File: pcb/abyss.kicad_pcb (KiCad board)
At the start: 2 copper layers, 137.5 x 111.5 mm, 36 parts

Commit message: Fix nets
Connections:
- D14 pad 1: R4 -> R3
- D15 pad 1: R4 -> R3
- D16 pad 1: R4 -> R3

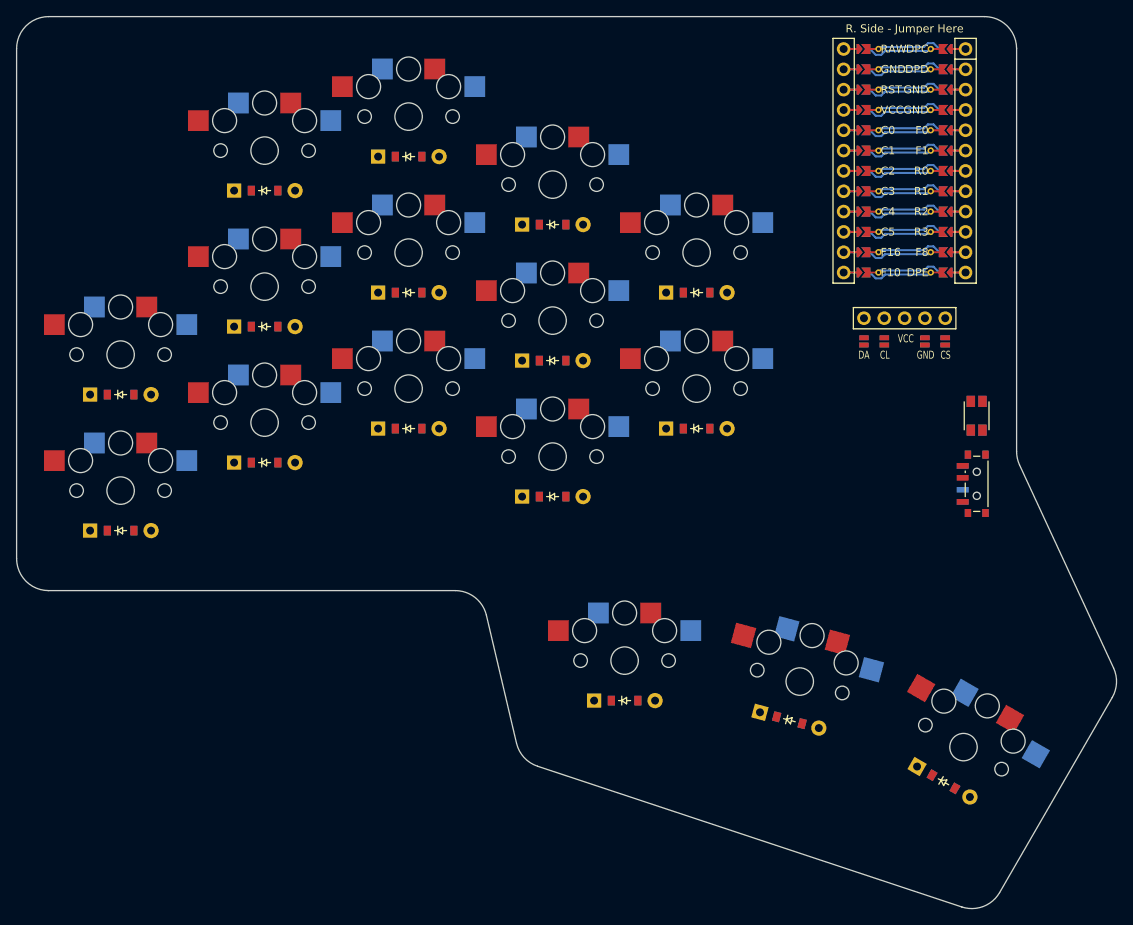
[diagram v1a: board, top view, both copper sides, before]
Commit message: Add battery jst and cleanup layout
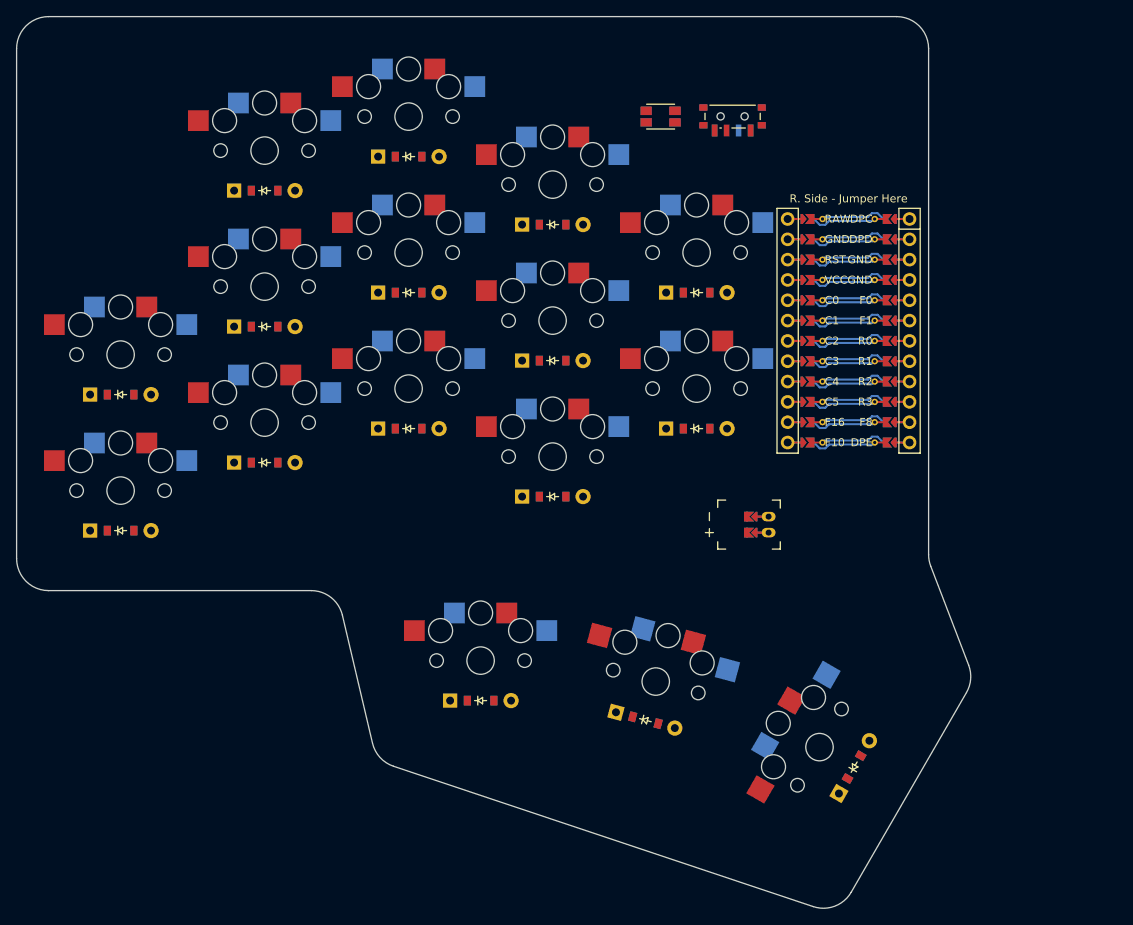
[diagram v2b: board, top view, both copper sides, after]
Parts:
- removed DISP1: , nice!view
- added JST1: , ceoloide/battery_connector_jst_ph_2, F.Cu at (181.0, 104.2)
- moved SW2 55.1 mm to (176.5, 53.2), turned to 90 degrees
- moved SW1 54.4 mm to (167.5, 53.2), turned to 90 degrees
- moved MCU1 22.4 mm to (191.0, 78.8)
- moved D14 18.0 mm to (145.0, 126.2)
- moved D15 18.0 mm to (165.6, 128.7)
- moved S14 18.0 mm to (145.0, 121.2)
- moved S15 18.0 mm to (166.9, 123.9)
- moved S16 18.0 mm to (187.4, 132.1), turned to 60 degrees
- moved D16 11.3 mm to (191.7, 134.6), turned to 60 degrees
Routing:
- net JST1_2: track 0.00 -> 3.60 mm
- net JST1_1: track 0.00 -> 3.60 mm
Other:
- board size 137.5 x 111.5 mm -> 119.3 x 111.5 mm

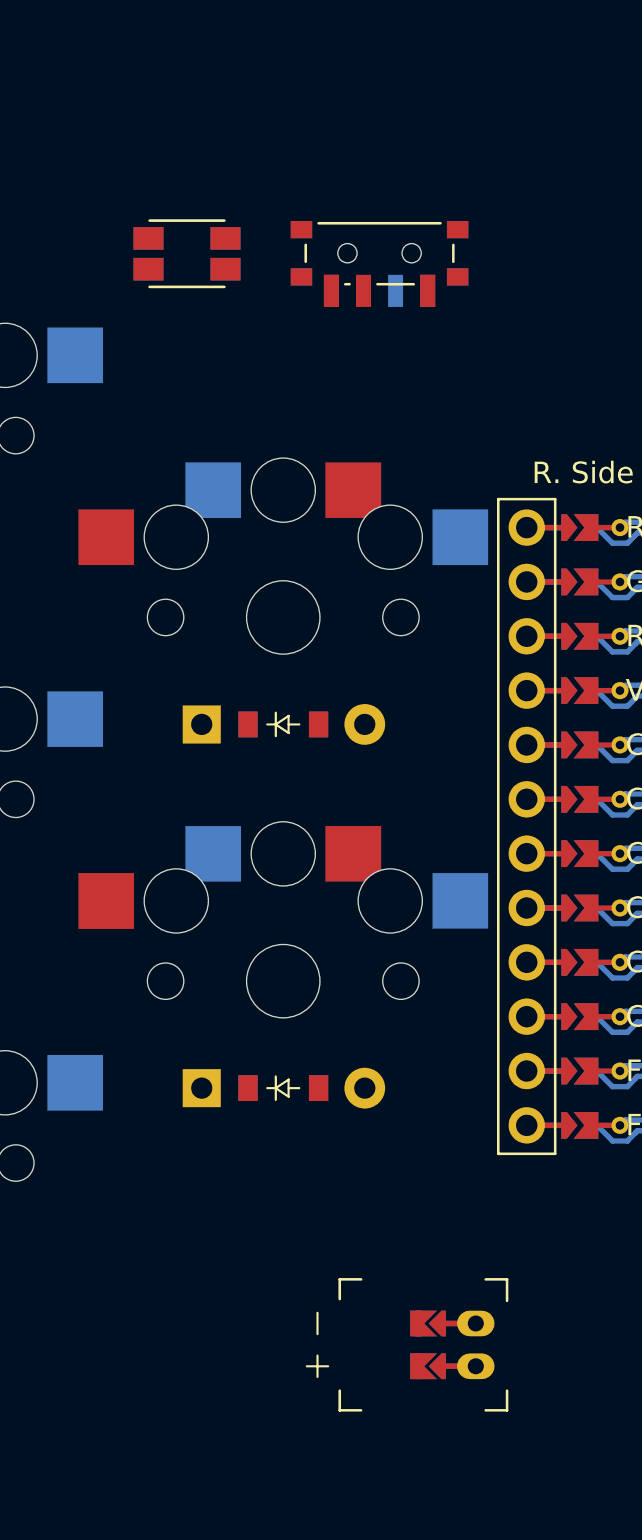
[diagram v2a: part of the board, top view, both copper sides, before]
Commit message: Move jst connector at the top
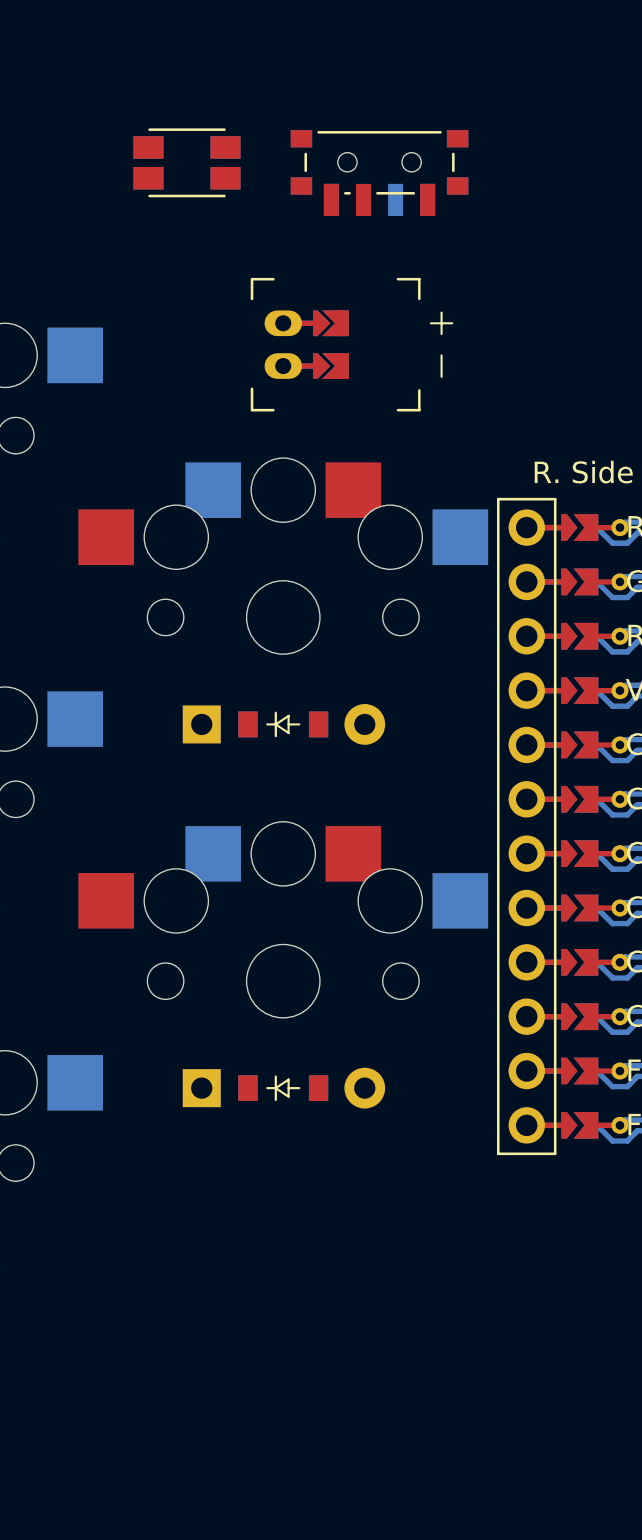
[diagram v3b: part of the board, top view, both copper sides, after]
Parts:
- moved JST1 47.6 mm to (172.0, 57.5), turned to 90 degrees
- moved SW1 4.25 mm to (167.5, 49.0)
- moved SW2 4.25 mm to (176.5, 49.0)
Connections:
- D1 pad 1: R0 -> R2
- D11 pad 1: R2 -> R0
- D12 pad 1: R0 -> R2
- D3 pad 1: R0 -> R2
- D5 pad 1: R2 -> R0
- D6 pad 1: R0 -> R2
- D8 pad 1: R2 -> R0
- D9 pad 1: R0 -> R2
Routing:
- net R2: track 0.00 -> 50.9 mm
- net R0: track 50.9 -> 0.00 mm

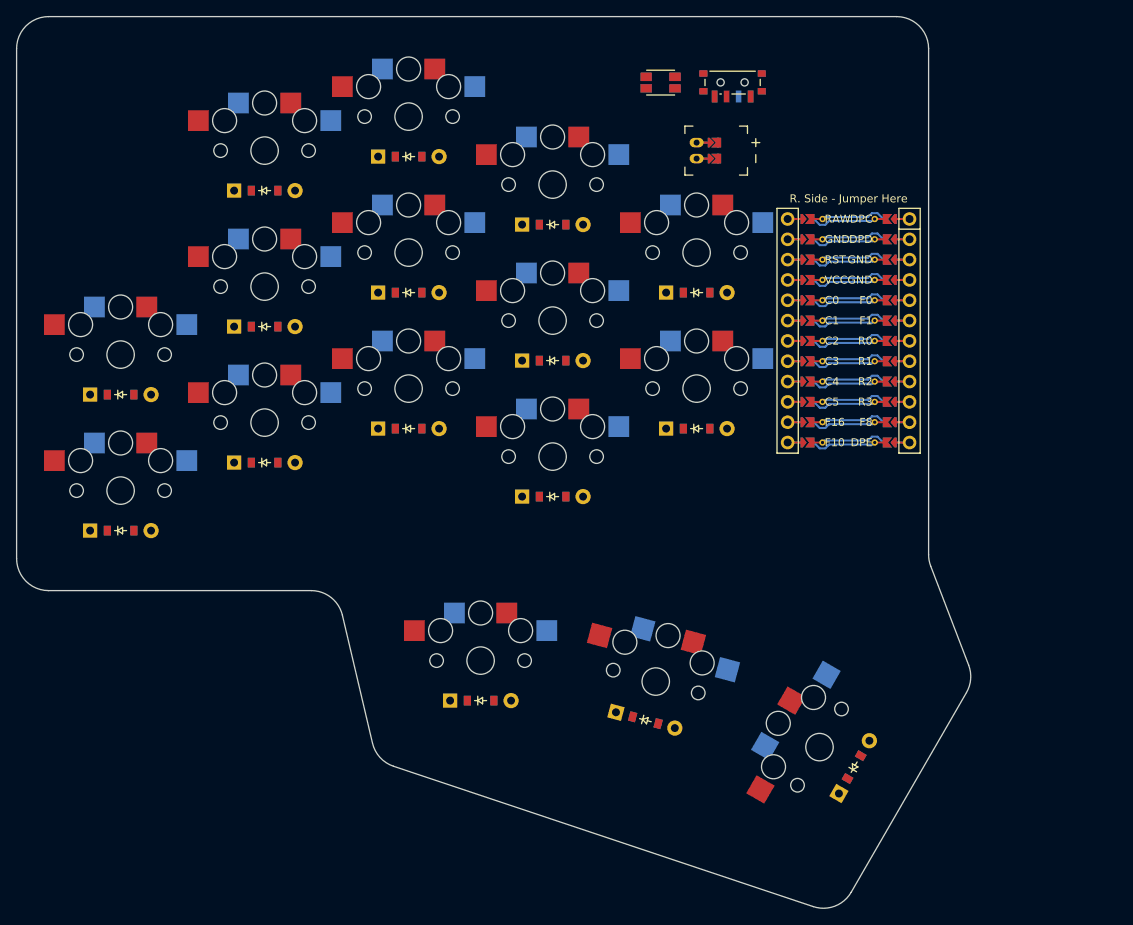
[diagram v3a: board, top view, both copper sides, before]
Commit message: Add mounting holes on the pcb
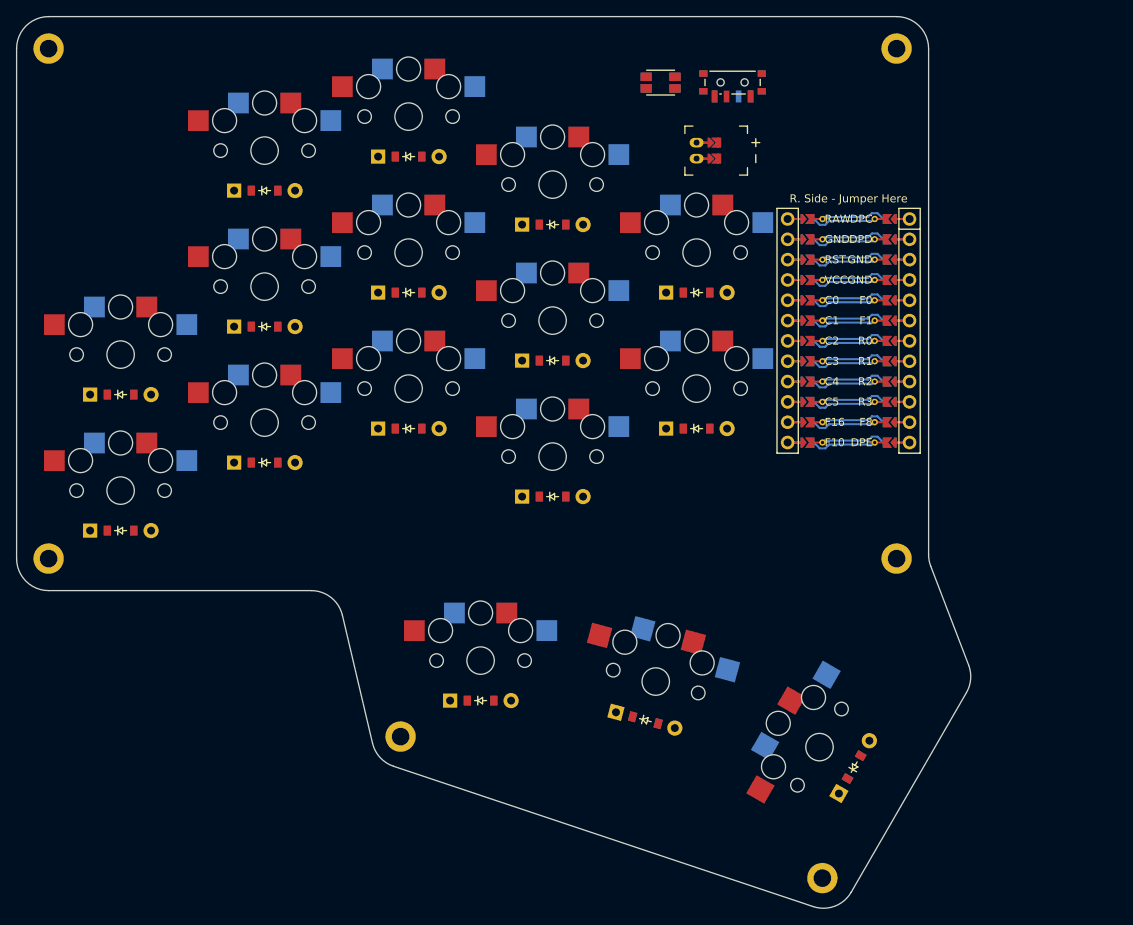
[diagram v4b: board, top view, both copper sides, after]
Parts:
- added H1: , mounting_hole, F.Cu at (91.0, 44.8)
- added H2: , mounting_hole, F.Cu at (197.0, 44.8)
- added H3: , mounting_hole, F.Cu at (197.0, 108.5)
- added H4: , mounting_hole, F.Cu at (91.0, 108.5)
- added H5: , mounting_hole, F.Cu at (135.0, 130.8)
- added H6: , mounting_hole, F.Cu at (187.7, 148.4)
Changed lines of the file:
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@@
         (segment (start 173.800 56.500) (end 172.000 56.500) (width 0.25) (layer "F.Cu") (net 65))
         (segment (start 173.800 56.500) (end 172.000 56.500) (width 0.25) (layer "B.Cu") (net 65))
+            (module mounting_hole (layer F.Cu)
+                (at 91 44.75 0)
+                (fp_text reference "H1" (at 0 3) (layer F.SilkS) hide
+                    (effects (font (size 1 1) (thickness 0.15)))
+                )
+                (pad "" thru_hole circle (at 0 0 180) (size 3.8000000000000003 3.8000000000000003) (drill 2.2) (layers *.Cu *.Mask))
+                (fp_circle (center 0 0) (end -2.1500000000000004 0) (layer F.CrtYd) (width 0.05))
+                (fp_circle (center 0 0) (end -2.1500000000000004 0) (layer B.CrtYd) (width 0.05))
+            )
+            (module mounting_hole (layer F.Cu)
+                (at 197 44.75 0)
+                (fp_text reference "H2" (at 0 3) (layer F.SilkS) hide
+                    (effects (font (size 1 1) (thickness 0.15)))
+                )
+                (pad "" thru_hole circle (at 0 0 180) (size 3.8000000000000003 3.8000000000000003) (drill 2.2) (layers *.Cu *.Mask))
+                (fp_circle (center 0 0) (end -2.1500000000000004 0) (layer F.CrtYd) (width 0.05))
+                (fp_circle (center 0 0) (end -2.1500000000000004 0) (layer B.CrtYd) (width 0.05))
+            )
+            (module mounting_hole (layer F.Cu)
+                (at 197 108.5 0)
+                (fp_text reference "H3" (at 0 3) (layer F.SilkS) hide
+                    (effects (font (size 1 1) (thickness 0.15)))
+                )
+                (pad "" thru_hole circle (at 0 0 180) (size 3.8000000000000003 3.8000000000000003) (drill 2.2) (layers *.Cu *.Mask))
+                (fp_circle (center 0 0) (end -2.1500000000000004 0) (layer F.CrtYd) (width 0.05))
+                (fp_circle (center 0 0) (end -2.1500000000000004 0) (layer B.CrtYd) (width 0.05))
+            )
+            (module mounting_hole (layer F.Cu)
+                (at 91 108.5 0)
+                (fp_text reference "H4" (at 0 3) (layer F.SilkS) hide
+                    (effects (font (size 1 1) (thickness 0.15)))
+                )
+                (pad "" thru_hole circle (at 0 0 180) (size 3.8000000000000003 3.8000000000000003) (drill 2.2) (layers *.Cu *.Mask))
+                (fp_circle (center 0 0) (end -2.1500000000000004 0) (layer F.CrtYd) (width 0.05))
+                (fp_circle (center 0 0) (end -2.1500000000000004 0) (layer B.CrtYd) (width 0.05))
+            )
+            (module mounting_hole (layer F.Cu)
+                (at 135 130.75 0)
+                (fp_text reference "H5" (at 0 3) (layer F.SilkS) hide
+                    (effects (font (size 1 1) (thickness 0.15)))
+                )
+                (pad "" thru_hole circle (at 0 0 180) (size 3.8000000000000003 3.8000000000000003) (drill 2.2) (layers *.Cu *.Mask))
+                (fp_circle (center 0 0) (end -2.1500000000000004 0) (layer F.CrtYd) (width 0.05))
+                (fp_circle (center 0 0) (end -2.1500000000000004 0) (layer B.CrtYd) (width 0.05))
+            )
+            (module mounting_hole (layer F.Cu)
+                (at 187.72396099999997 148.4395207 60)
+                (fp_text reference "H6" (at 0 3) (layer F.SilkS) hide
+                    (effects (font (size 1 1) (thickness 0.15)))
+                )
+                (pad "" thru_hole circle (at 0 0 180) (size 3.8000000000000003 3.8000000000000003) (drill 2.2) (layers *.Cu *.Mask))
+                (fp_circle (center 0 0) (end -2.1500000000000004 0) (layer F.CrtYd) (width 0.05))
+                (fp_circle (center 0 0) (end -2.1500000000000004 0) (layer B.CrtYd) (width 0.05))
+            )
             (gr_line (start 87 108.5) (end 87 44.75) (angle 90) (layer Edge.Cuts) (width 0.15))
 (gr_line (start 91 40.75) (end 197 40.75) (angle 90) (layer Edge.Cuts) (width 0.15))
